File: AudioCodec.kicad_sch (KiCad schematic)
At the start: 21 parts, among them U1 WM8904CGEFL/V

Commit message: Finalized schematic
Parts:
- removed C13, C14: 4.7u, symbol Device:C_Small
- removed C5: 0.1uF, symbol Device:C_Small
- added J5: Conn_01x02, symbol Connector_Generic:Conn_01x02
- added TP1 (x6): TestPoint, TestPoint:TestPoint_Pad_1.5x1.5mm, symbol Connector:TestPoint
- C1, C10, C11, C12, C2, C3, C4, C6, C7, C8, C9: footprint (none) -> Capacitor_SMD:C_0402_1005Metric
- R3, R4, R5, R6, R7, R8: footprint (none) -> Resistor_SMD:R_0402_1005Metric
- U1: footprint QFN32_4X4_CIR -> TeenieWeenieLibrary:QFN32_4X4_CIR
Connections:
- net AUDIOIN1_L: now also TP1.1
- net AUDIOIN1_R: now also TP1.1
- net AUDIOIN2_L: now also TP1.1
- net AUDIOIN2_R: now also TP1.1
- net LINEOUTL: now also TP1.1
- net LINEOUTR: now also TP1.1
- net at C10.2: now also J5.2 (Pin_2)
- net at C9.2: now also J5.1 (Pin_1)
- net DUT_MICBIAS: no longer names the net of U1.20 (MICBIAS)
- net DUT_VMIDC: no longer names the net of U1.21 (VMIDC)
- net MICVDD: no longer names the net of U1.19 (MICVDD)
- no-connect marks 2 -> 5

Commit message: final final schematic:
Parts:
- removed J5: Conn_01x02, symbol Connector_Generic:Conn_01x02
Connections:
- net AudioOut_R: now reaches C10.2
- net AudioOut_L: now reaches C9.2
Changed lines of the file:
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@@
     (effects (font (size 1.27 1.27)) (justify left bottom))
+  )
+  (hierarchical_label "AudioOut_R" (shape output) (at 160.02 142.24 0) (fields_autoplaced)
+    (effects (font (size 1.27 1.27)) (justify left))
   )
   (hierarchical_label "MCLK" (shape bidirectional) (at 181.61 87.63 0) (fields_autoplaced)
@@
   (hierarchical_label "SCKL" (shape bidirectional) (at 88.9 77.47 180) (fields_autoplaced)
     (effects (font (size 1.27 1.27)) (justify right))
+  )
+  (hierarchical_label "AudioOut_L" (shape output) (at 160.02 139.7 0) (fields_autoplaced)
+    (effects (font (size 1.27 1.27)) (justify left))
   )
   (hierarchical_label "AUDIOIN2_R" (shape bidirectional) (at 229.87 97.79 0) (fields_autoplaced)
@@
         )
       )
-    )
-  )
-  (symbol (lib_id "Connector_Generic:Conn_01x02") (at 165.1 139.7 0) (unit 1)
-    (in_bom yes) (on_board yes) (dnp no) (fields_autoplaced)
-    (property "Reference" "J5" (at 167.64 139.7 0)
-      (effects (font (size 1.27 1.27)) (justify left))
-    )
-    (property "Value" "Conn_01x02" (at 167.64 142.24 0)
-      (effects (font (size 1.27 1.27)) (justify left))
-    )
-    (property "Footprint" "" (at 165.1 139.7 0)
-      (effects (font (size 1.27 1.27)) hide)
-    )
-    (property "Datasheet" "~" (at 165.1 139.7 0)
-      (effects (font (size 1.27 1.27)) hide)
-    )
-    (pin "1")
-    (pin "2")
-    (instances
-      (project "TeenieWeenie"
-        (path "/58e2e2d3-cf30-4313-be51-7fb67401d242/f0c54189-8a5f-41c5-ac40-c182d77a5377"
-          (reference "J5") (unit 1)
-        )
-      )

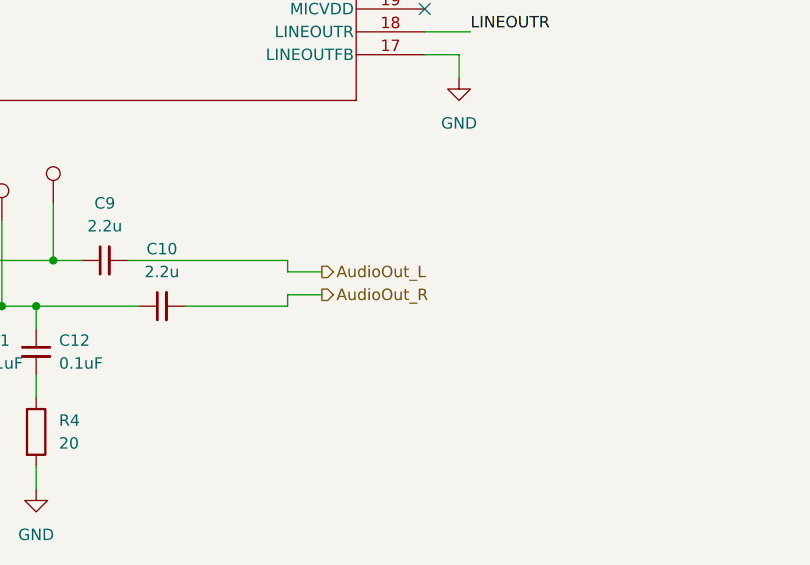
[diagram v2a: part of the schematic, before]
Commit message: routed power
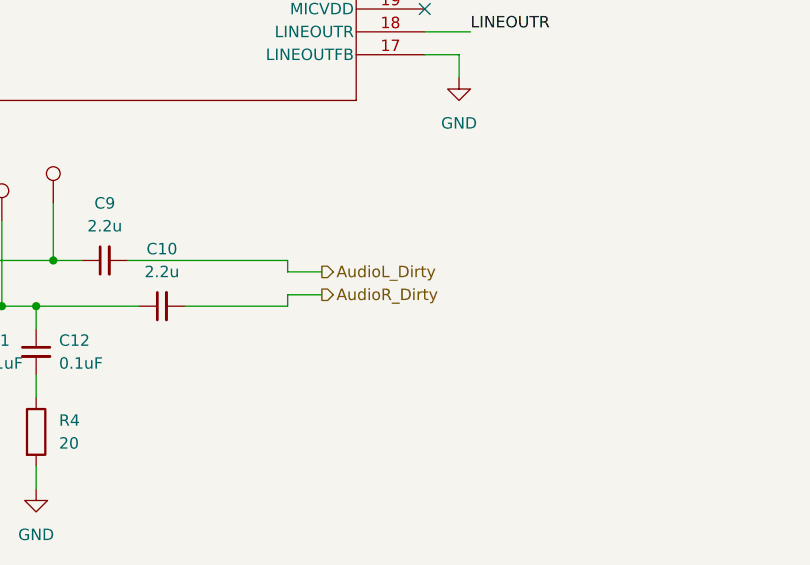
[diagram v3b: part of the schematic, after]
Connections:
- net AudioOut_L renamed AudioL_Dirty
- net AudioOut_R renamed AudioR_Dirty
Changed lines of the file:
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@@
     (effects (font (size 1.27 1.27)) (justify left bottom))
   )
-  (hierarchical_label "AudioOut_R" (shape output) (at 160.02 142.24 0) (fields_autoplaced)
+  (hierarchical_label "AudioR_Dirty" (shape output) (at 160.02 142.24 0) (fields_autoplaced)
     (effects (font (size 1.27 1.27)) (justify left))
   )
@@
     (effects (font (size 1.27 1.27)) (justify right))
   )
-  (hierarchical_label "AudioOut_L" (shape output) (at 160.02 139.7 0) (fields_autoplaced)
+  (hierarchical_label "AudioL_Dirty" (shape output) (at 160.02 139.7 0) (fields_autoplaced)
     (effects (font (size 1.27 1.27)) (justify left))
   )

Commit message: redesign layout
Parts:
- C10, C9: value 2.2u -> 4.7u
- R6, R8, TP1: now not fitted
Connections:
- net at U1.24 (IN2R): no longer R8.1
- net at U1.26 (IN2L): no longer R6.1
- no-connect marks 5 -> 9
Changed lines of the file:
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@@
   (no_connect (at 100.33 105.41))
   (no_connect (at 171.45 105.41))
+  (no_connect (at 171.45 92.71))
+  (no_connect (at 204.47 92.71))
+  (no_connect (at 171.45 97.79))
+  (no_connect (at 217.17 97.79))
   (wire (pts (xy 171.45 115.57) (xy 175.26 115.57))
     (stroke (width 0) (type default))
@@
     (stroke (width 0) (type default))
   )
-  (wire (pts (xy 171.45 97.79) (xy 217.17 97.79))
-    (stroke (width 0) (type default))
-  )
   (wire (pts (xy 144.78 143.51) (xy 156.21 143.51))
     (stroke (width 0) (type default))
@@
   )
   (wire (pts (xy 72.39 36.83) (xy 72.39 39.37))
-    (stroke (width 0) (type default))
-  )
-  (wire (pts (xy 171.45 92.71) (xy 204.47 92.71))
     (stroke (width 0) (type default))
   )
@@
   )
   (symbol (lib_id "Connector:TestPoint") (at 228.6 69.85 0) (unit 1)
-    (in_bom yes) (on_board yes) (dnp no) (fields_autoplaced)
+    (in_bom yes) (on_board no) (dnp yes) (fields_autoplaced)
     (property "Reference" "TP1" (at 231.14 65.278 0)
       (effects (font (size 1.27 1.27)) (justify left))
@@
   )
   (symbol (lib_id "Device:R") (at 220.98 97.79 90) (unit 1)
-    (in_bom yes) (on_board yes) (dnp no)
+    (in_bom yes) (on_board no) (dnp yes)
     (property "Reference" "R8" (at 220.98 92.71 90)
       (effects (font (size 1.27 1.27)))
@@
   )
   (symbol (lib_id "Connector:TestPoint") (at 213.36 77.47 0) (unit 1)
-    (in_bom yes) (on_board yes) (dnp no) (fields_autoplaced)
+    (in_bom yes) (on_board no) (dnp yes) (fields_autoplaced)
     (property "Reference" "TP1" (at 215.9 72.898 0)
       (effects (font (size 1.27 1.27)) (justify left))
@@
       (effects (font (size 1.27 1.27)))
     )
-    (property "Value" "2.2u" (at 142.2463 139.7 90)
+    (property "Value" "4.7u" (at 142.2463 139.7 90)
       (effects (font (size 1.27 1.27)))
     )
@@
   )
   (symbol (lib_id "Device:R") (at 208.28 92.71 90) (unit 1)
-    (in_bom yes) (on_board yes) (dnp no)
+    (in_bom yes) (on_board no) (dnp yes)
     (property "Reference" "R6" (at 208.28 87.63 90)
       (effects (font (size 1.27 1.27)))
@@
       (effects (font (size 1.27 1.27)))
     )
-    (property "Value" "2.2u" (at 135.8963 134.62 90)
-      (effects (font (size 1.27 1.27)))
-    )
+    (property "Value" "4.7u" (at 135.8963 134.62 90)
+      (effects (font (size 1.27 1.27)))
+    )
